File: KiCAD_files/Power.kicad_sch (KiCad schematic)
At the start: 64 parts, among them J101 2604-1102, J102 2604-1102, J103 2604-1102, J104 2604-1102, J105 2604-1102, U101 AMC1311, U102 OPA316, U103 OPA316, U104 +-20A

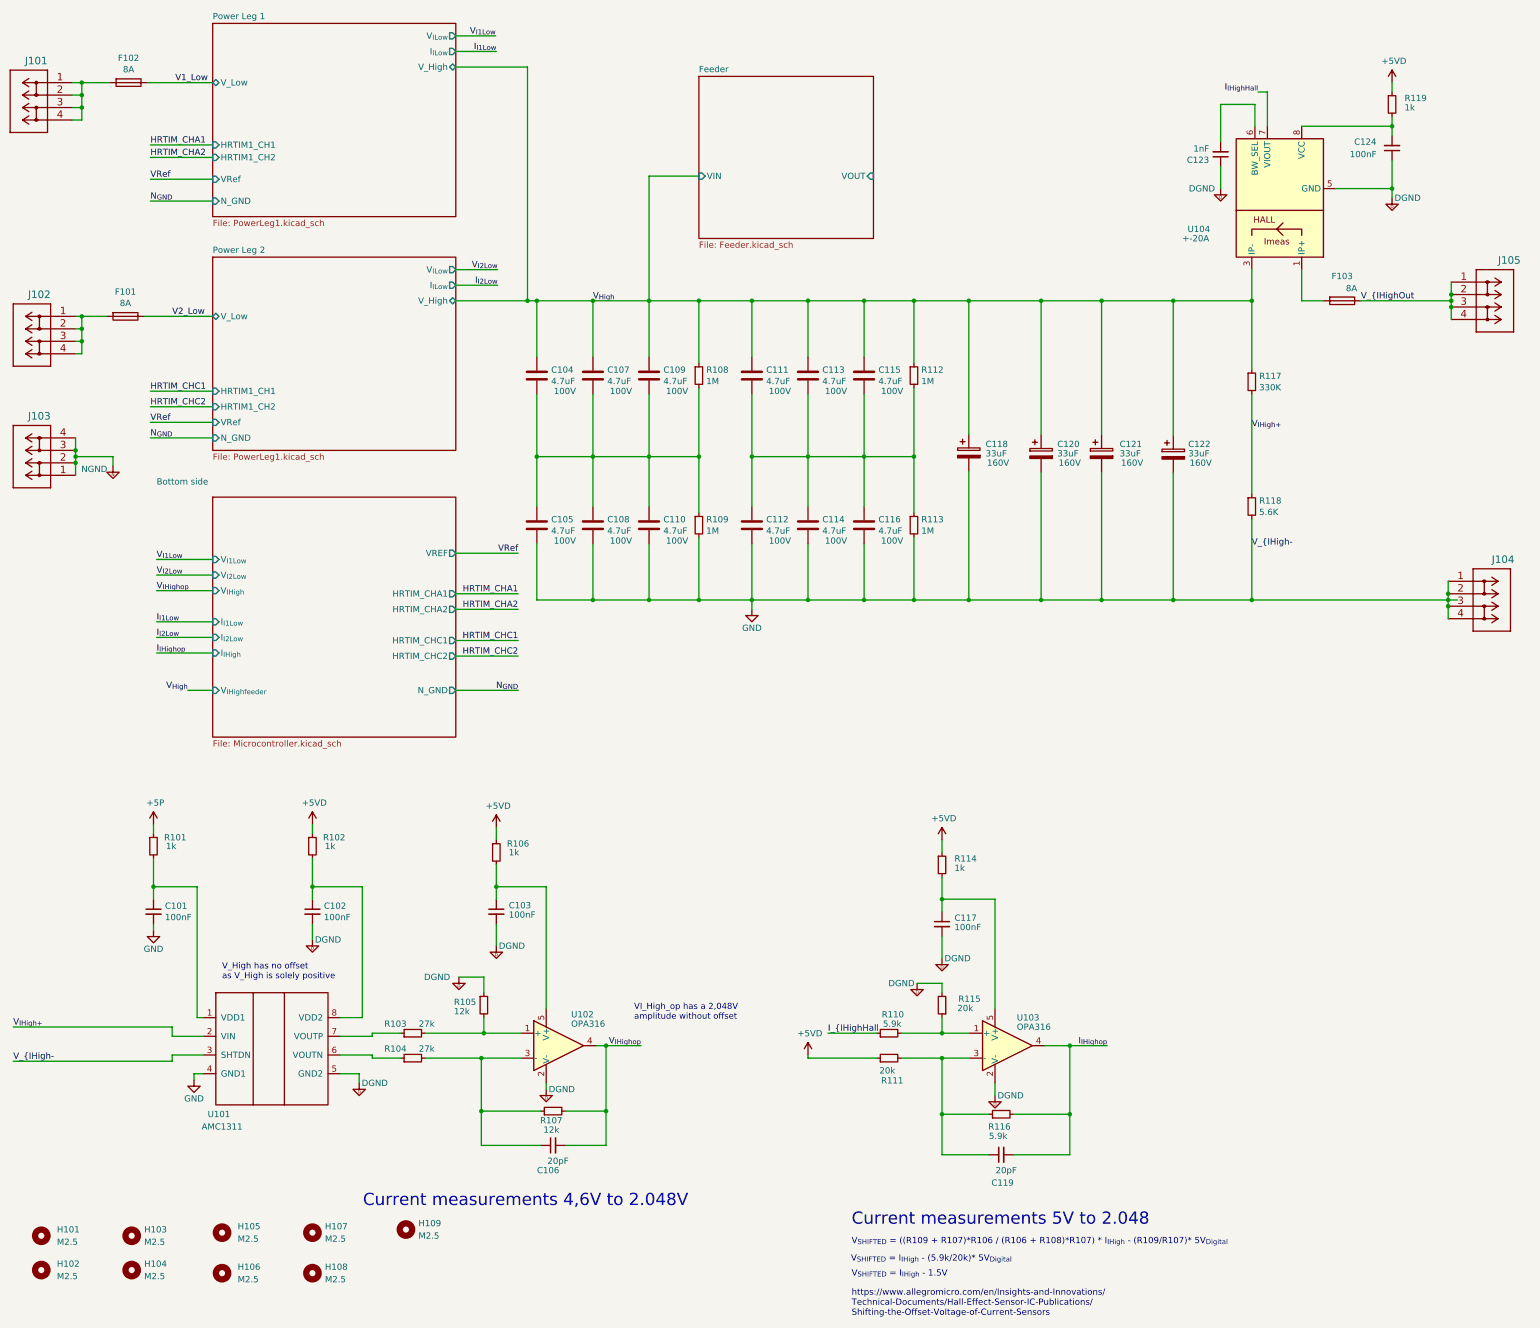
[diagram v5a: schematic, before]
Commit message: WIP : Routed last sensors to the MCU, tweaked the courtiyards ERC almost passing
Former-commit-id: ade1cde8d39341e78235fc8e83a4a1c667a0d829
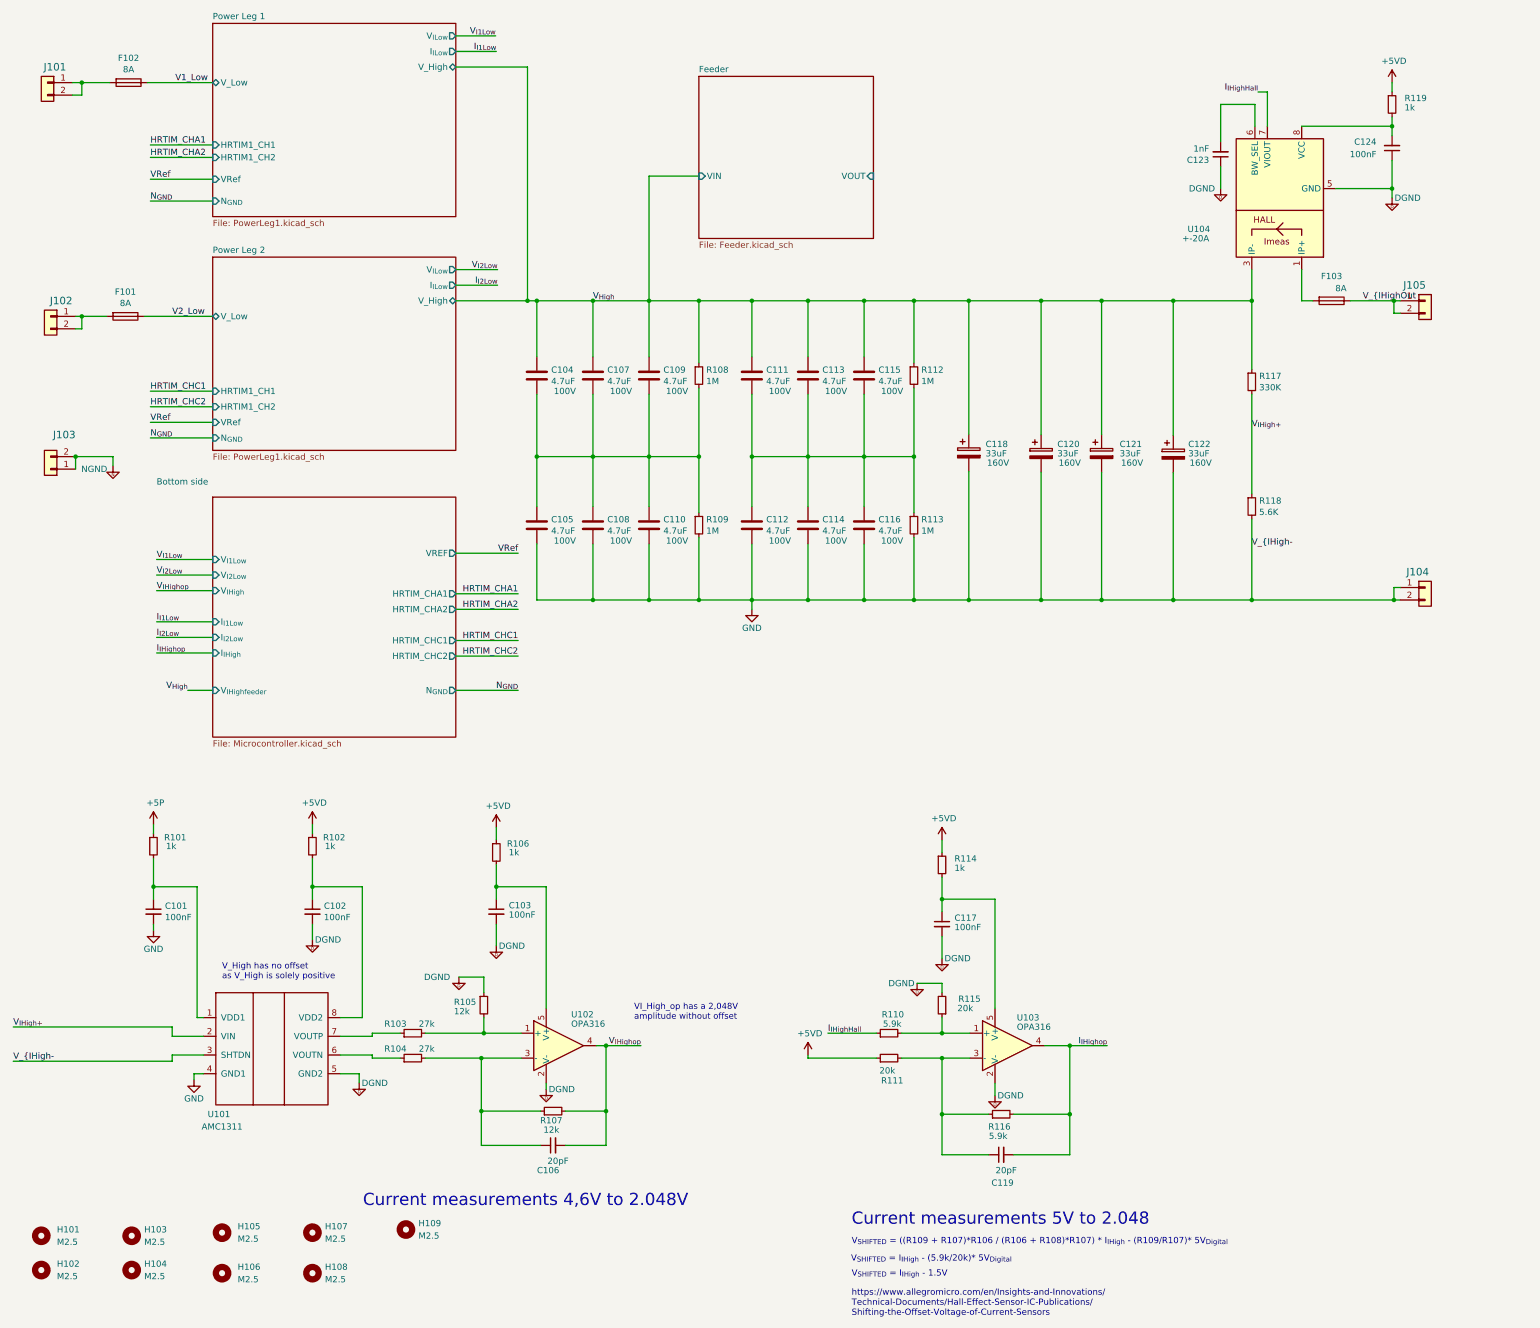
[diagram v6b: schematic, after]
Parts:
- C103, C106, C117, C119, C123: footprint Capacitor_SMD:C_0805_2012Metric -> Footprints:C_0805_2012Metric
- C104, C105, C107, C108, C109, C110, C111, C112, C113, C114, C115, C116: footprint Capacitor_SMD:C_1210_3225Metric -> Footprints:C_1210_3225Metric
- J101, J102, J103, J104, J105: symbol Symbols:2604-1102 -> Connector_Generic:Conn_01x02
- R101, R102, R103, R104, R105, R106, R107, R108, R109, R110, R111, R112, R113, R114, R115, R116, R117, R118, R119: footprint Resistor_SMD:R_0805_2012Metric -> Footprints:R_0805_2012Metric
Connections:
- net I_{IHighHall is gone; now on net I_{IHighHall}: R110.1
- net GND: no longer J104.3, J104.4
- net NGND: no longer J103.3, J103.4
- net V_{IHighOut: no longer J105.3, J105.4
- net at F101.2, J102.1 (Pin_1), J102.2 (Pin_2): no longer J102.3, J102.4
- net at F102.2, J101.1 (Pin_1), J101.2 (Pin_2): no longer J101.3, J101.4
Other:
- sheet Bottom side ports: added N_{GND}; removed N_GND
- sheet Power Leg 1 ports: added N_{GND}; removed N_GND
- sheet Power Leg 2 ports: added N_{GND}; removed N_GND
- moved on the sheet: F103

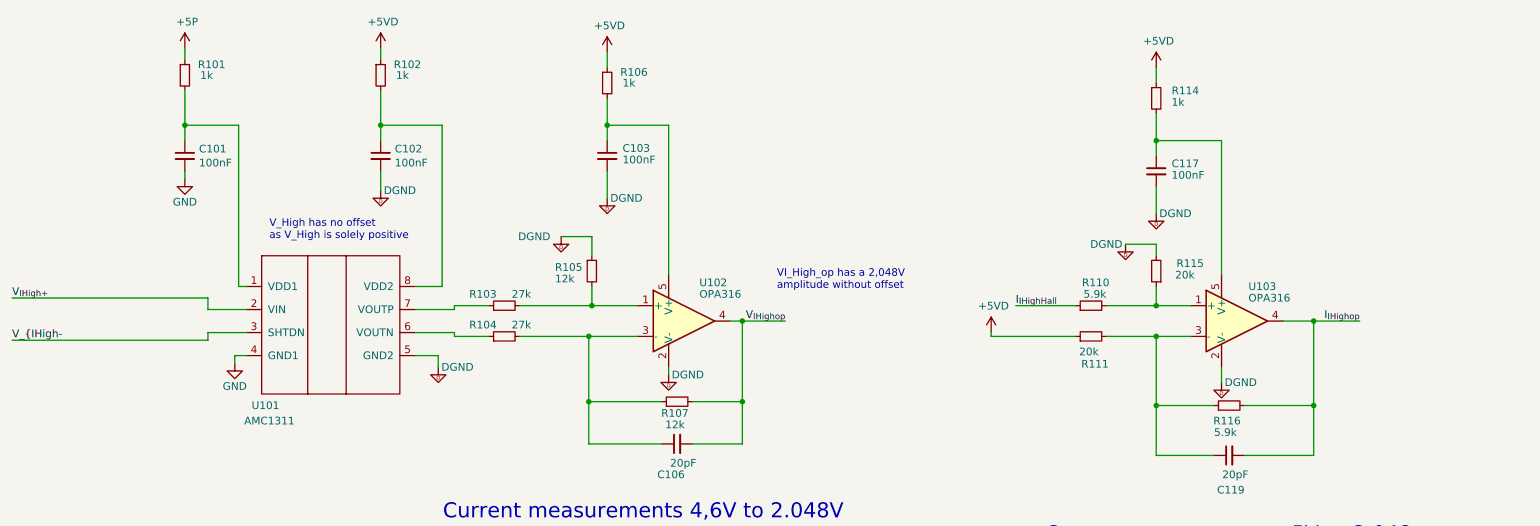
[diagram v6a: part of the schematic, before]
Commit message: WIP : Started correcting MCU board mistakes
Former-commit-id: 0e34b6d72e10d1eac13c8cf31fc8e8f14d7f468b
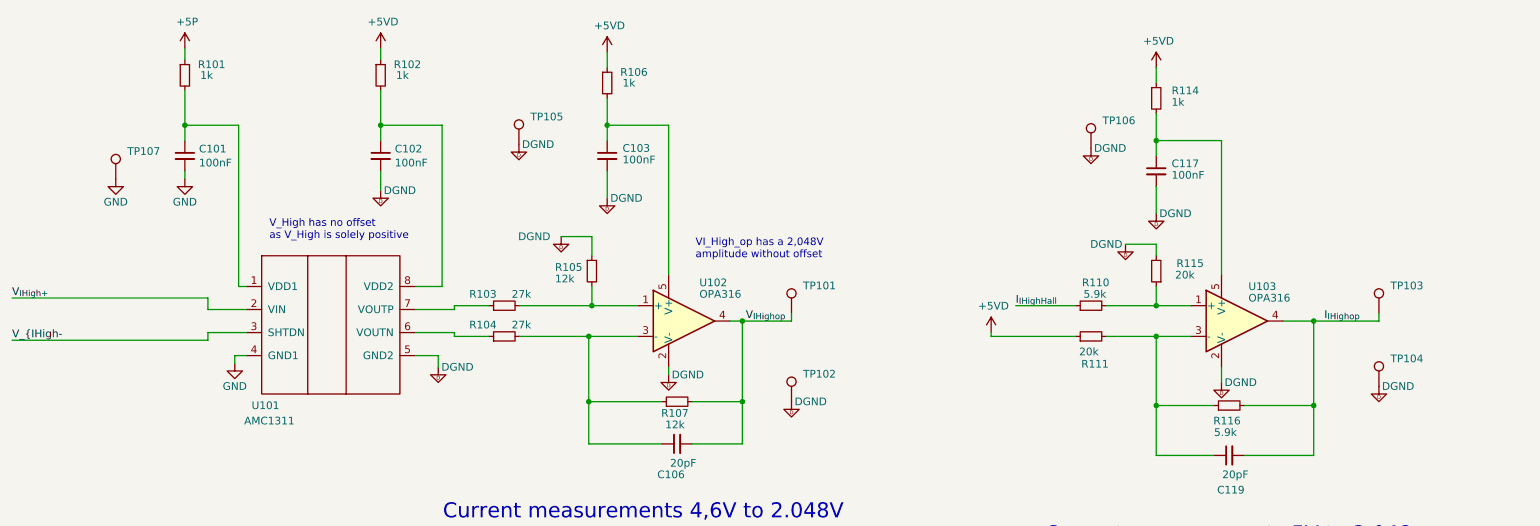
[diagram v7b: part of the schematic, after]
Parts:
- added TP101, TP102, TP103, TP104, TP105, TP106, TP107: TestPoint, TestPoint:TestPoint_Pad_D1.0mm, symbol Connector:TestPoint
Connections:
- net DGND: now also TP102.1, TP104.1, TP105.1, TP106.1
- net GND: now also TP107.1
- net I_{IHighop}: now also TP103.1
- net V_{IHighop}: now also TP101.1

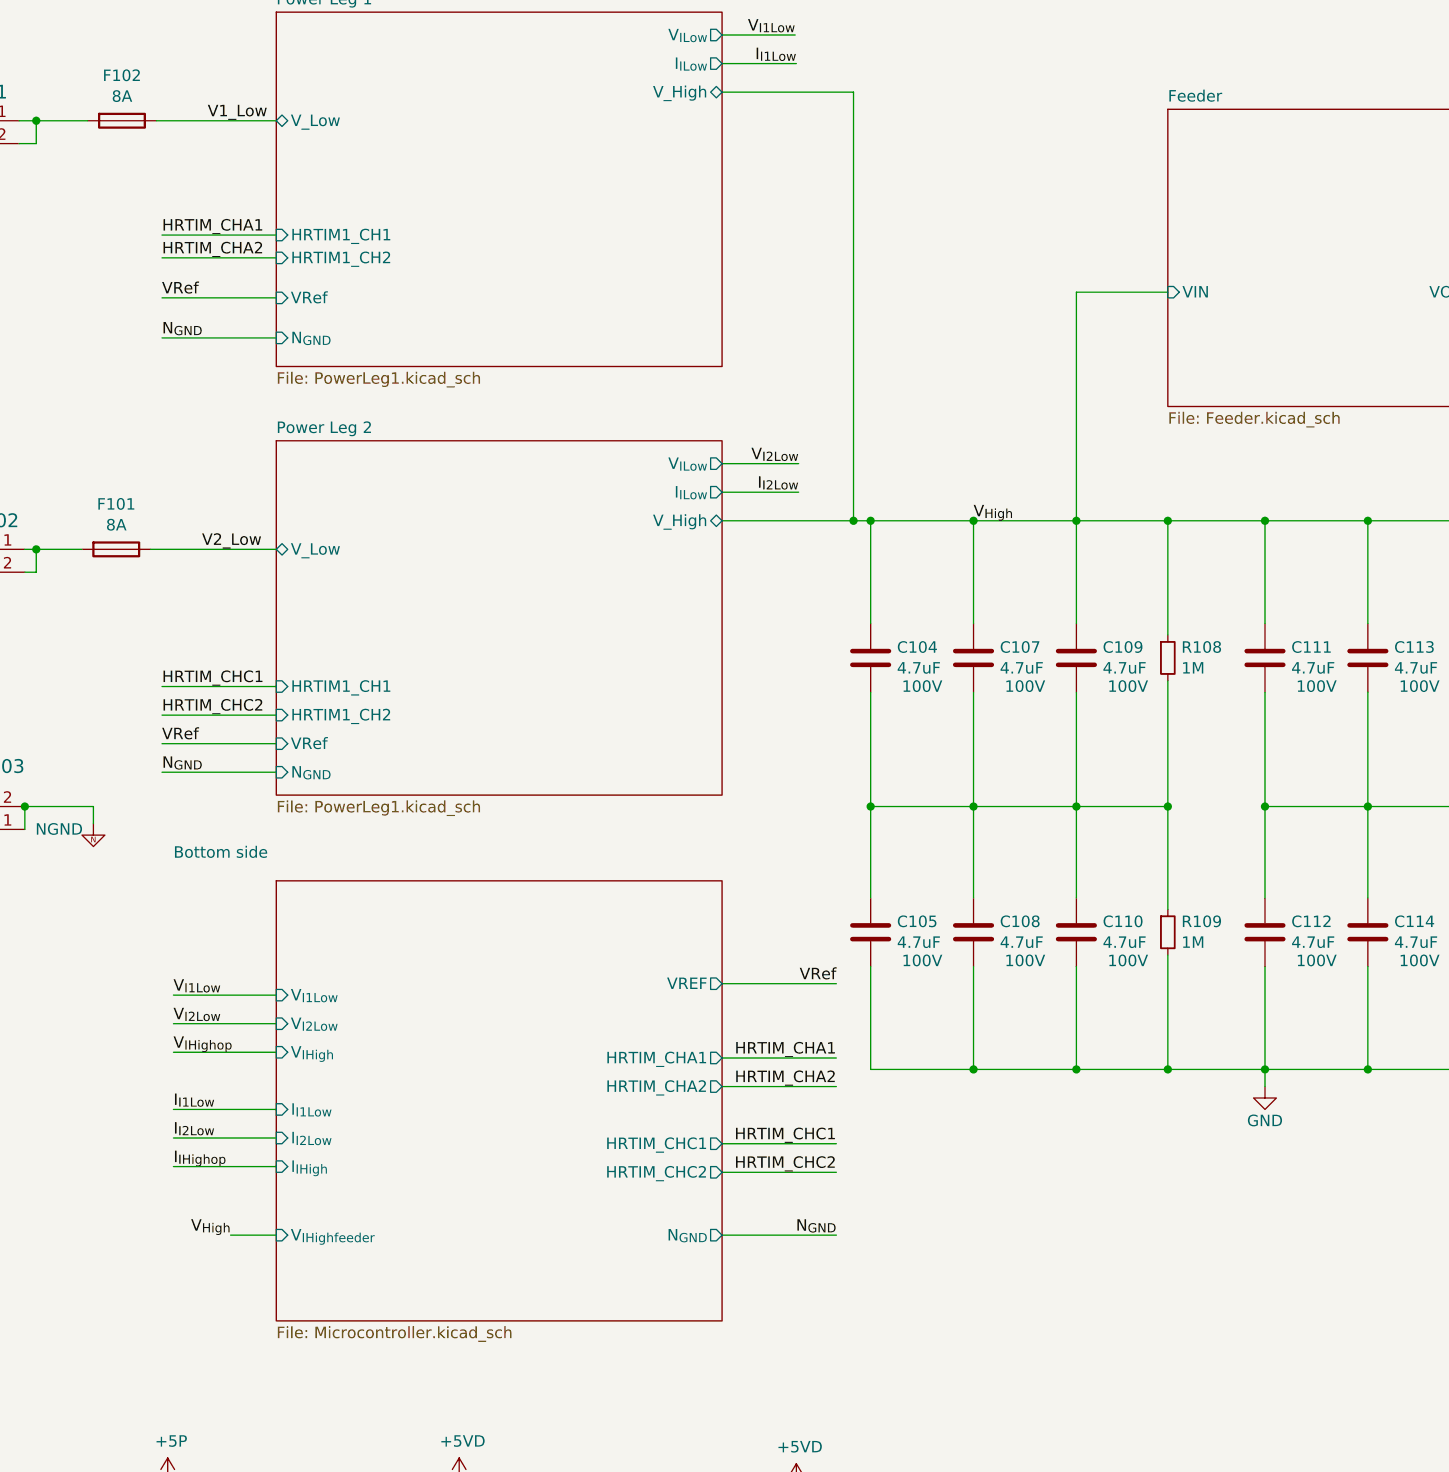
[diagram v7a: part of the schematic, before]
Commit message: WIP: added features for the RJ45 communication link. Added fast RS485 Added HRTIM Sync Added current share analog bus Added external VREF Added dedicated supply power supply pins for the data manager
Former-commit-id: 7d7dbd6688aaf47caa2ea5f91bf9cef552f6a24c
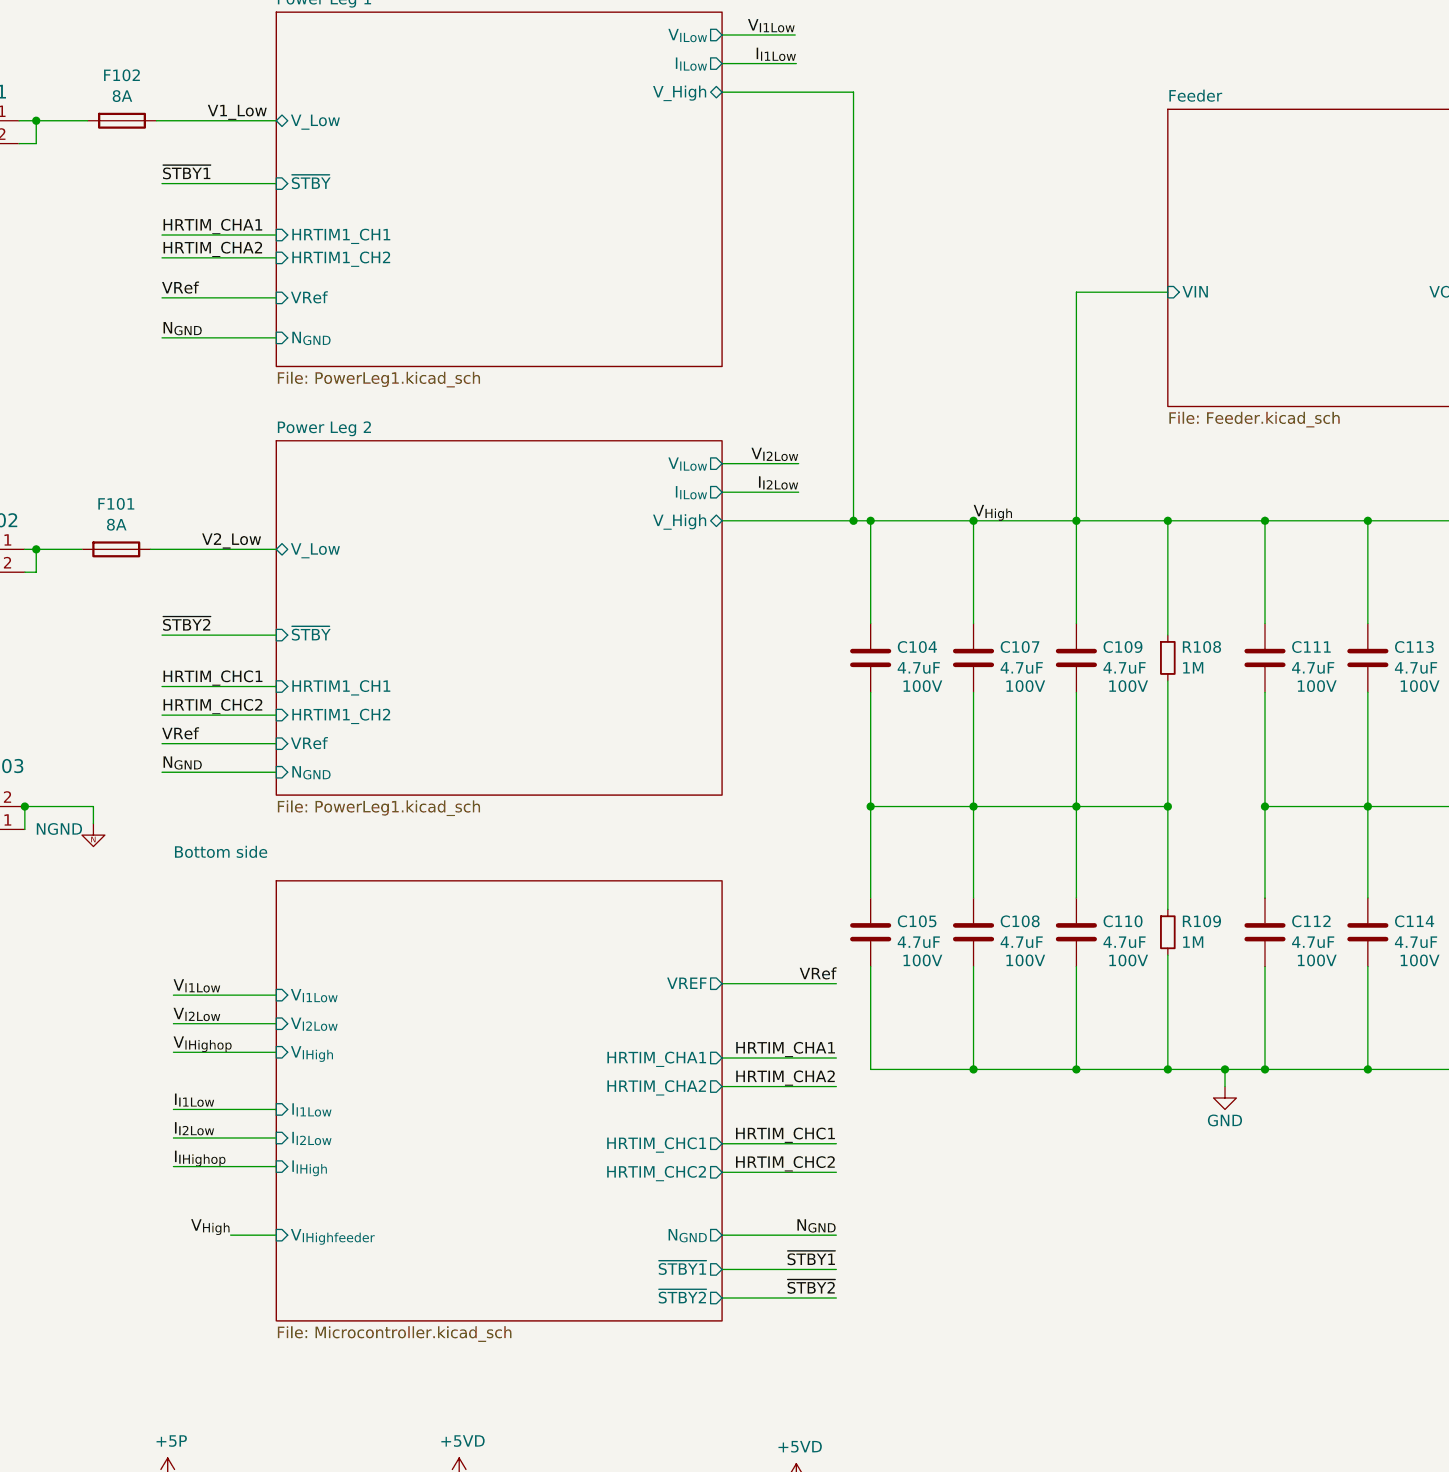
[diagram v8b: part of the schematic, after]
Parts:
- TP101, TP102, TP103, TP104, TP105, TP106, TP107: footprint TestPoint:TestPoint_Pad_D1.0mm -> Footprints:TestPoint_THTPad_D1.5mm_Drill0.7mm
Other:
- sheet Bottom side ports: added ~{STBY1}, ~{STBY2}; removed none
- sheet Power Leg 1 ports: added ~{STBY}; removed none
- sheet Power Leg 2 ports: added ~{STBY}; removed none
